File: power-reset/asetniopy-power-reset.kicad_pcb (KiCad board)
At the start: 2 copper layers, 32.3 x 8.4 mm, 5 parts, among them J1 Conn_01x03_Female, SW1 Reset, SW2 Power

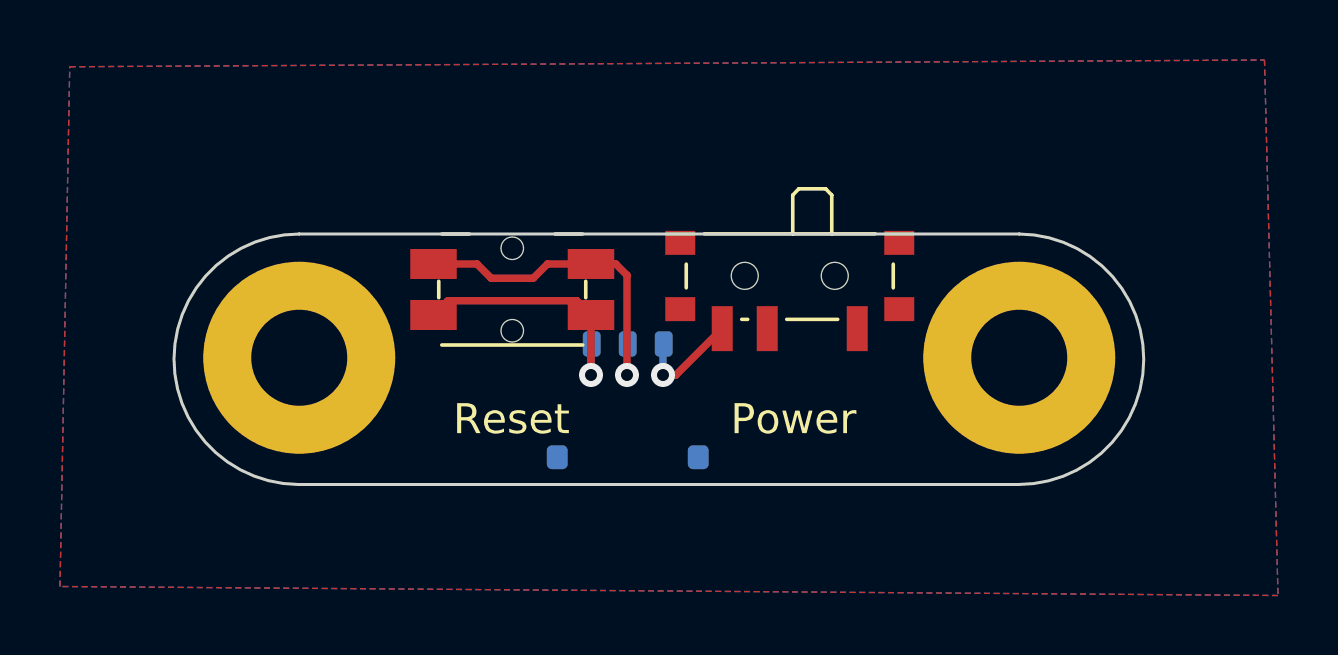
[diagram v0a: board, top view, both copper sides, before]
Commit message: Enlarge power/reset enough for JLC assembly.
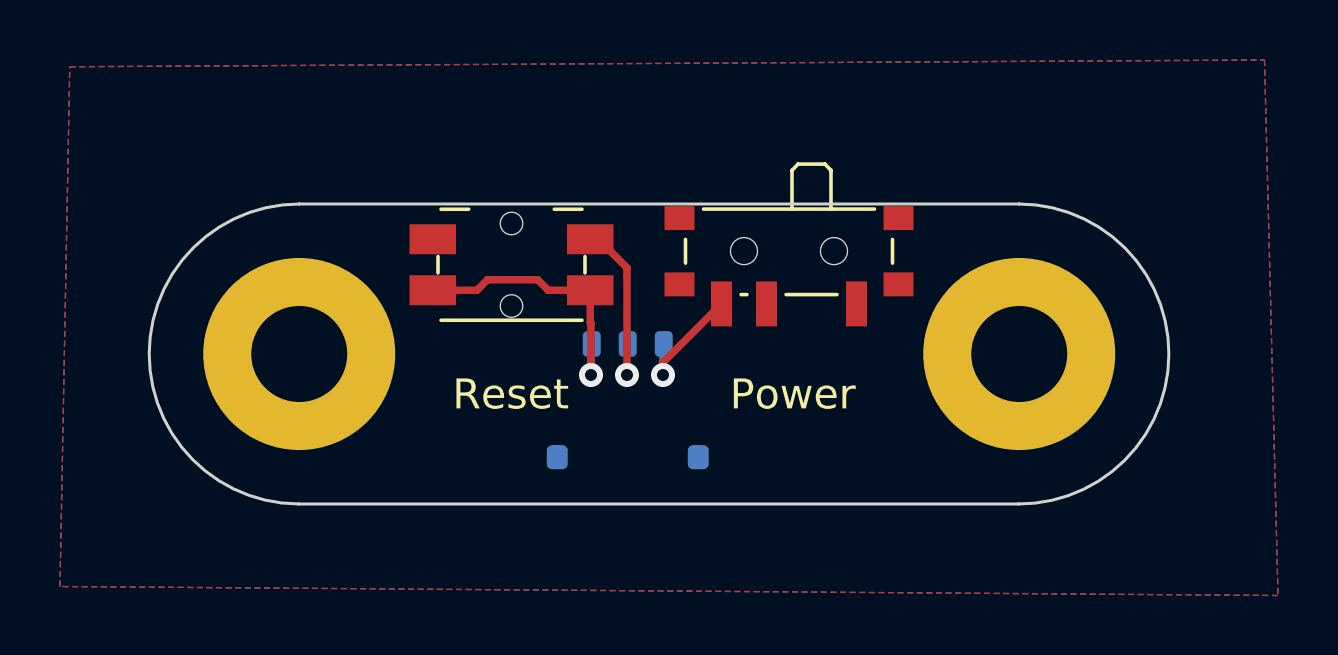
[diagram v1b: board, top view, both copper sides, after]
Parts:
- moved SW1 0.83 mm to (142.2, 83.0)
- moved SW2 0.83 mm to (151.5, 82.9)
- moved H1 0.13 mm to (135.2, 86.0)
- moved H2 0.13 mm to (159.2, 86.0)
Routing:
- net GND: track 10.4 -> 5.23 mm
- net RESET: track 8.69 -> 9.42 mm
- net BAT-: track 3.66 -> 4.22 mm
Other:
- board size 32.3 x 8.4 mm -> 34 x 10 mm
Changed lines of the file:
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@@
   (net 4 "unconnected-(SW2-Pad1)")
   (footprint "MountingHole:MountingHole_3.2mm_M3_Pad" (layer "F.Cu")
-    (at 159.15 86.125074)
+    (at 159.15 86)
     (descr "Mounting Hole 3.2mm, M3")
     (tags "mounting hole 3.2mm m3")
@@
   )
   (footprint "Button_Switch_SMD:SW_SPDT_PCM12" (layer "F.Cu")
-    (at 151.5 83.725 180)
+    (at 151.475 82.9 180)
     (descr "Ultraminiature Surface Mount Slide Switch, right-angle, https://www.ckswitches.com/media/1424/pcm.pdf")
     (property "Sheetfile" "asetniopy-power-reset.kicad_sch")
@@
   )
   (footprint "Button_Switch_SMD:Panasonic_EVQPUL_EVQPUC" (layer "F.Cu")
-    (at 142.25 83.85)
+    (at 142.225 83.025)
     (descr "http://industrial.panasonic.com/cdbs/www-data/pdf/ATV0000/ATV0000CE5.pdf")
     (tags "SMD SMT SPST EVQPUL EVQPUC")
@@
   )
   (footprint "MountingHole:MountingHole_3.2mm_M3_Pad" (layer "F.Cu")
-    (at 135.15 86.125074)
+    (at 135.15 86)
     (descr "Mounting Hole 3.2mm, M3")
     (tags "mounting hole 3.2mm m3")
@@
     )
   )
-  (gr_arc (start 159.15 82.000001) (mid 163.300055 86.1875) (end 159.125 90.350074) (layer "Edge.Cuts") (width 0.1))
-  (gr_line (start 159.15 82) (end 135.15 82) (layer "Edge.Cuts") (width 0.1))
-  (gr_arc (start 135.125 90.350073) (mid 130.974945 86.162574) (end 135.15 82) (layer "Edge.Cuts") (width 0.1))
-  (gr_line (start 159.125 90.350074) (end 135.125 90.350074) (layer "Edge.Cuts") (width 0.1))
-  (segment (start 139.625 84.7) (end 140.1 84.225) (width 0.25) (layer "F.Cu") (net 1))
-  (segment (start 144.875 86.7) (end 144.875 84.7) (width 0.25) (layer "F.Cu") (net 1))
-  (segment (start 144.4 84.225) (end 144.875 84.7) (width 0.25) (layer "F.Cu") (net 1))
-  (segment (start 140.1 84.225) (end 144.4 84.225) (width 0.25) (layer "F.Cu") (net 1))
+  (gr_arc (start 159.15 81) (mid 164.137873 86.0125) (end 159.125 91) (layer "Edge.Cuts") (width 0.1))
+  (gr_line (start 159.15 81) (end 135.15 81) (layer "Edge.Cuts") (width 0.1))
+  (gr_arc (start 135.125 91) (mid 130.148393 85.987527) (end 135.15 81) (layer "Edge.Cuts") (width 0.1))
+  (gr_line (start 159.125 91) (end 135.125 91) (layer "Edge.Cuts") (width 0.1))
+  (segment (start 144.85 83.875) (end 143.45 83.875) (width 0.25) (layer "F.Cu") (net 1))
+  (segment (start 144.875 86.7) (end 144.875 84.975) (width 0.25) (layer "F.Cu") (net 1))
+  (segment (start 144.85 84.95) (end 144.85 83.875) (width 0.25) (layer "F.Cu") (net 1))
+  (segment (start 144.875 84.975) (end 144.85 84.95) (width 0.25) (layer "F.Cu") (net 1))
+  (segment (start 141.075 83.875) (end 139.6 83.875) (width 0.25) (layer "F.Cu") (net 1))
+  (segment (start 141.425 83.525) (end 141.075 83.875) (width 0.25) (layer "F.Cu") (net 1))
+  (segment (start 143.1 83.525) (end 141.425 83.525) (width 0.25) (layer "F.Cu") (net 1))
+  (segment (start 143.45 83.875) (end 143.1 83.525) (width 0.25) (layer "F.Cu") (net 1))
   (via (at 144.875 86.7) (size 0.8) (drill 0.4) (layers "F.Cu" "B.Cu") (net 1))
   (segment (start 144.875 86.7) (end 144.875 85.690724) (width 0.25) (layer "B.Cu") (net 1))
   (segment (start 144.875 85.690724) (end 144.9 85.665724) (width 0.25) (layer "B.Cu") (net 1))
   (segment (start 146.075 86.7) (end 146.075 83.375) (width 0.25) (layer "F.Cu") (net 2))
-  (segment (start 142.95 83.475) (end 143.425 83) (width 0.25) (layer "F.Cu") (net 2))
-  (segment (start 146.075 83.375) (end 145.7 83) (width 0.25) (layer "F.Cu") (net 2))
-  (segment (start 143.425 83) (end 144.875 83) (width 0.25) (layer "F.Cu") (net 2))
-  (segment (start 141.075 83) (end 141.55 83.475) (width 0.25) (layer "F.Cu") (net 2))
-  (segment (start 145.7 83) (end 144.875 83) (width 0.25) (layer "F.Cu") (net 2))
-  (segment (start 139.625 83) (end 141.075 83) (width 0.25) (layer "F.Cu") (net 2))
-  (segment (start 141.55 83.475) (end 142.95 83.475) (width 0.25) (layer "F.Cu") (net 2))
+  (segment (start 146.075 83.125) (end 145.125 82.175) (width 0.25) (layer "F.Cu") (net 2))
+  (segment (start 145.125 82.175) (end 144.85 82.175) (width 0.25) (layer "F.Cu") (net 2))
+  (segment (start 146.075 83.375) (end 146.075 83.125) (width 0.25) (layer "F.Cu") (net 2))
   (via (at 146.075 86.7) (size 0.8) (drill 0.4) (layers "F.Cu" "B.Cu") (net 2))
   (segment (start 146.075 86.7) (end 146.1 86.725) (width 0.25) (layer "B.Cu") (net 2))
-  (segment (start 147.705 86.7) (end 149.25 85.155) (width 0.25) (layer "F.Cu") (net 3))
-  (segment (start 147.275 86.7) (end 147.705 86.7) (width 0.25) (layer "F.Cu") (net 3))
+  (segment (start 147.275 86.28) (end 149.225 84.33) (width 0.25) (layer "F.Cu") (net 3))
+  (segment (start 147.275 86.7) (end 147.275 86.28) (width 0.25) (layer "F.Cu") (net 3))
   (via (at 147.275 86.7) (size 0.8) (drill 0.4) (layers "F.Cu" "B.Cu") (net 3))
   (segment (start 147.275 85.690724) (end 147.3 85.665724) (width 0.25) (layer "B.Cu") (net 3))
